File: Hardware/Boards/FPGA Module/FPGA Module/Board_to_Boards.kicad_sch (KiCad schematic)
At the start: 0 parts

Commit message: FPGA Board schematic work
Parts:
- added J1, J2: LSHM-130-XX.X-XXX-DV-A-S-K-XX, FPGA Module:SAMTEC_LSHM-130-XX.X-XXX-DV-A-S-K-XX, symbol FPGA Module:LSHM-130-XX.X-XXX-DV-A-S-K-XX

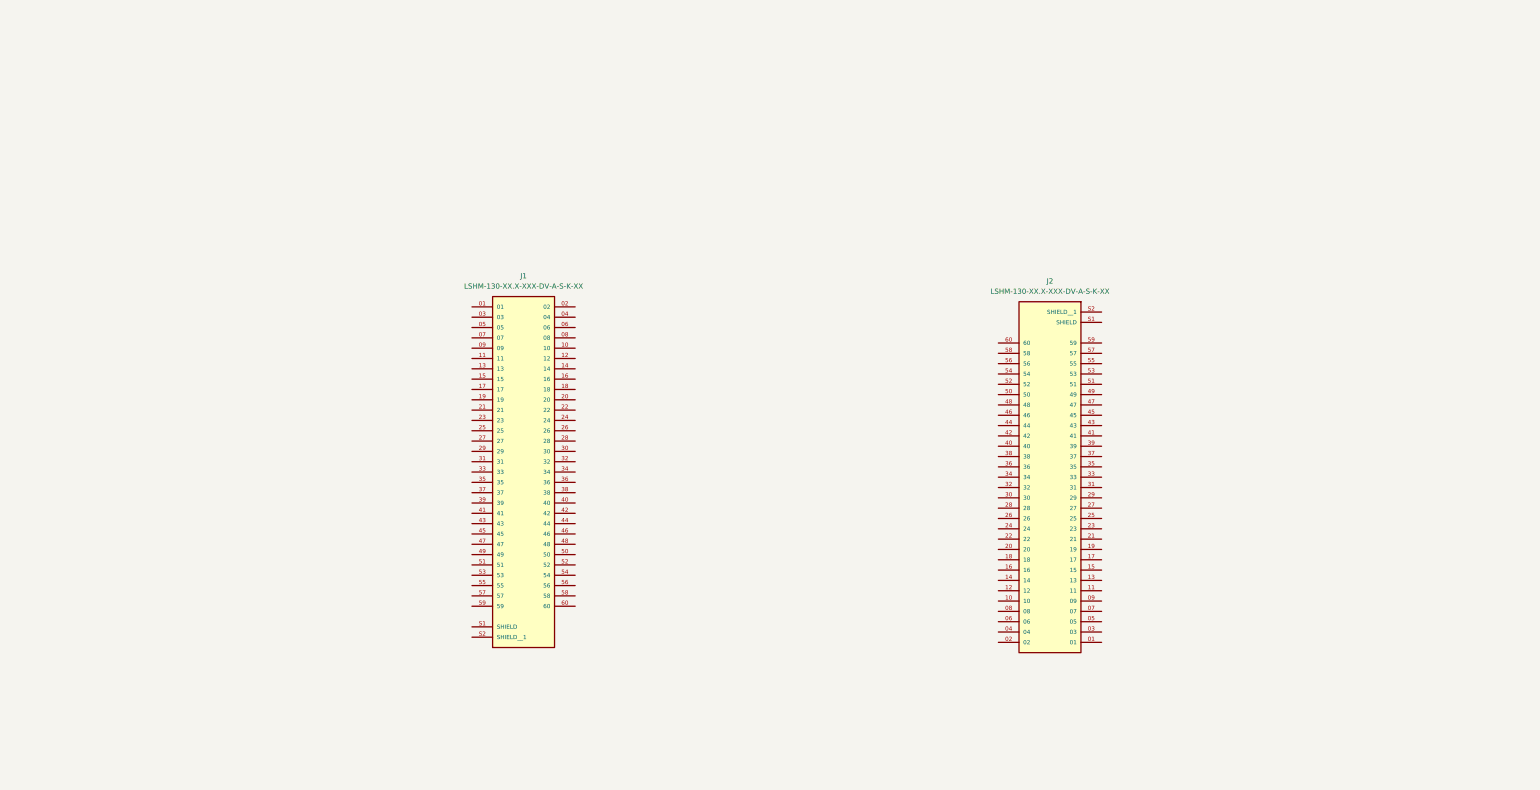
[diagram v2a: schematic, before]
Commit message: FPGA Module Schematic work
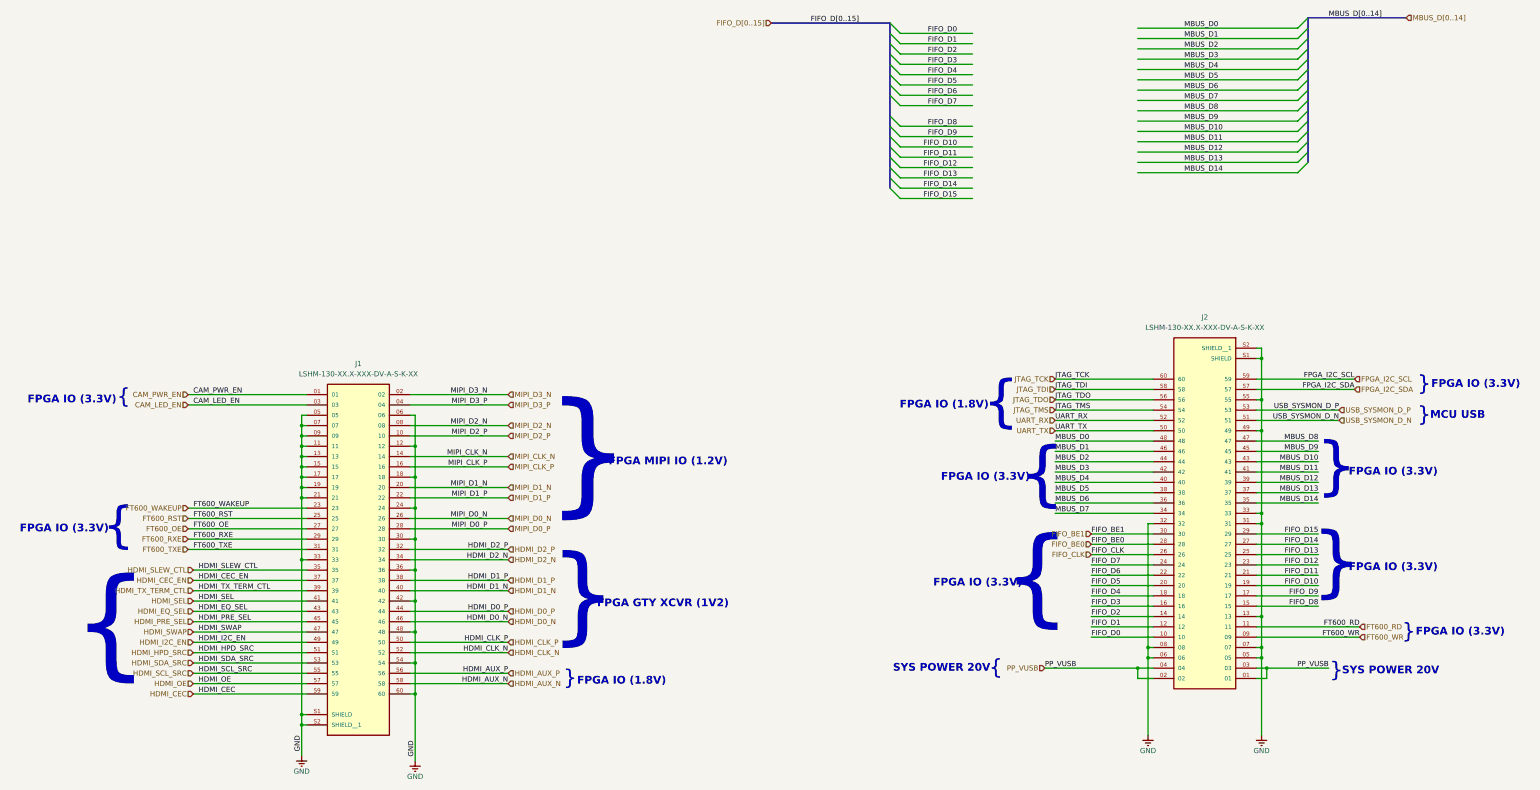
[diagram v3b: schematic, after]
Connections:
- net PP_VUSB: now reaches J2.01
- net PP_VUSB: now also J2.02, J2.03, J2.04
- net GND: now reaches J2.05
- net GND: now also J1.05, J1.06, J1.07, J1.09, J1.11, J1.12, J1.13, J1.15, J1.17, J1.18, J1.19, J1.21, J1.24, J1.30, J1.33, J1.36, J1.42, J1.48, J1.54, J1.60, J1.S1 (SHIELD), J1.S2 (SHIELD__1), J2.06, J2.07, J2.08, J2.13, J2.31, J2.32, J2.33, J2.49, J2.55, J2.S1 (SHIELD), J2.S2 (SHIELD__1)
- net FT600_WR: now reaches J2.09
- net FIFO_D0: now reaches J2.10
- net FT600_RD: now reaches J2.11
- net FIFO_D1: now reaches J2.12
- net FIFO_D2: now reaches J2.14
- net FIFO_D8: now reaches J2.15
- net FIFO_D3: now reaches J2.16
- net FIFO_D9: now reaches J2.17
- net FIFO_D4: now reaches J2.18
- net FIFO_D10: now reaches J2.19
- net FIFO_D5: now reaches J2.20
- net FIFO_D11: now reaches J2.21
- net FIFO_D6: now reaches J2.22
- net FIFO_D12: now reaches J2.23
- net FIFO_D7: now reaches J2.24
- net FIFO_D13: now reaches J2.25
- net FIFO_CLK: now reaches J2.26
- net FIFO_D14: now reaches J2.27
- net FIFO_BE0: now reaches J2.28
- net FIFO_D15: now reaches J2.29
- net FIFO_BE1: now reaches J2.30
- net MBUS_D7: now reaches J2.34
- net MBUS_D14: now reaches J2.35
- net MBUS_D6: now reaches J2.36
- net MBUS_D13: now reaches J2.37
- net MBUS_D5: now reaches J2.38
- net MBUS_D12: now reaches J2.39
- net MBUS_D4: now reaches J2.40
- net MBUS_D11: now reaches J2.41
- net MBUS_D3: now reaches J2.42
- net MBUS_D10: now reaches J2.43
- net MBUS_D2: now reaches J2.44
- net MBUS_D9: now reaches J2.45
- net MBUS_D1: now reaches J2.46
- net MBUS_D8: now reaches J2.47
- net MBUS_D0: now reaches J2.48
- net UART_TX: now reaches J2.50
- net USB_SYSMON_D_N: now reaches J2.51
- net UART_RX: now reaches J2.52
- net USB_SYSMON_D_P: now reaches J2.53
- net JTAG_TMS: now reaches J2.54
- net JTAG_TDO: now reaches J2.56
- net FPGA_I2C_SDA: now reaches J2.57
- net JTAG_TDI: now reaches J2.58
- net FPGA_I2C_SCL: now reaches J2.59
- net JTAG_TCK: now reaches J2.60
- net CAM_PWR_EN: now reaches J1.01
- net MIPI_D3_N: now reaches J1.02
- net CAM_LED_EN: now reaches J1.03
- net MIPI_D3_P: now reaches J1.04
- net MIPI_D2_N: now reaches J1.08
- net MIPI_D2_P: now reaches J1.10
- net MIPI_CLK_N: now reaches J1.14
- net MIPI_CLK_P: now reaches J1.16
- net MIPI_D1_N: now reaches J1.20
- net MIPI_D1_P: now reaches J1.22
- net FT600_WAKEUP: now reaches J1.23
- net FT600_RST: now reaches J1.25
- net MIPI_D0_N: now reaches J1.26
- net FT600_OE: now reaches J1.27
- net MIPI_D0_P: now reaches J1.28
- net FT600_RXE: now reaches J1.29
- net FT600_TXE: now reaches J1.31
- net HDMI_D2_P: now reaches J1.32
- net HDMI_D2_N: now reaches J1.34
- net HDMI_SLEW_CTL: now reaches J1.35
- net HDMI_CEC_EN: now reaches J1.37
- net HDMI_D1_P: now reaches J1.38
- net HDMI_TX_TERM_CTL: now reaches J1.39
- net HDMI_D1_N: now reaches J1.40
- net HDMI_SEL: now reaches J1.41
- net HDMI_EQ_SEL: now reaches J1.43
- net HDMI_D0_P: now reaches J1.44
- net HDMI_PRE_SEL: now reaches J1.45
- net HDMI_D0_N: now reaches J1.46
- net HDMI_SWAP: now reaches J1.47
- net HDMI_I2C_EN: now reaches J1.49
- net HDMI_CLK_P: now reaches J1.50
- net HDMI_HPD_SRC: now reaches J1.51
- net HDMI_CLK_N: now reaches J1.52
- net HDMI_SDA_SRC: now reaches J1.53
- net HDMI_SCL_SRC: now reaches J1.55
- net HDMI_AUX_P: now reaches J1.56
- net HDMI_OE: now reaches J1.57
- net HDMI_AUX_N: now reaches J1.58
- net HDMI_CEC: now reaches J1.59
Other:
- note added: "FPGA GTY XCVR (1V2)"
- note added: "FPGA IO (1.8V)"
- note added: "FPGA IO (3.3V)"
- note added: "FPGA MIPI IO (1.2V)"
- note added: "MCU USB"
- note added: "SYS POWER 20V"
- note added: "{"
- note added: "}"
- moved on the sheet: J1, J2

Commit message: Using new DP to HDMI IC
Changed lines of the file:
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@@
+		)
+	)
+	(text "FPGA IO (1.8V)"
+		(exclude_from_sim no)
+		(at 34.29 177.8 0)
+		(effects
+			(font
+				(size 1.905 1.905)
+				(bold yes)
+			)
 		)
 	)

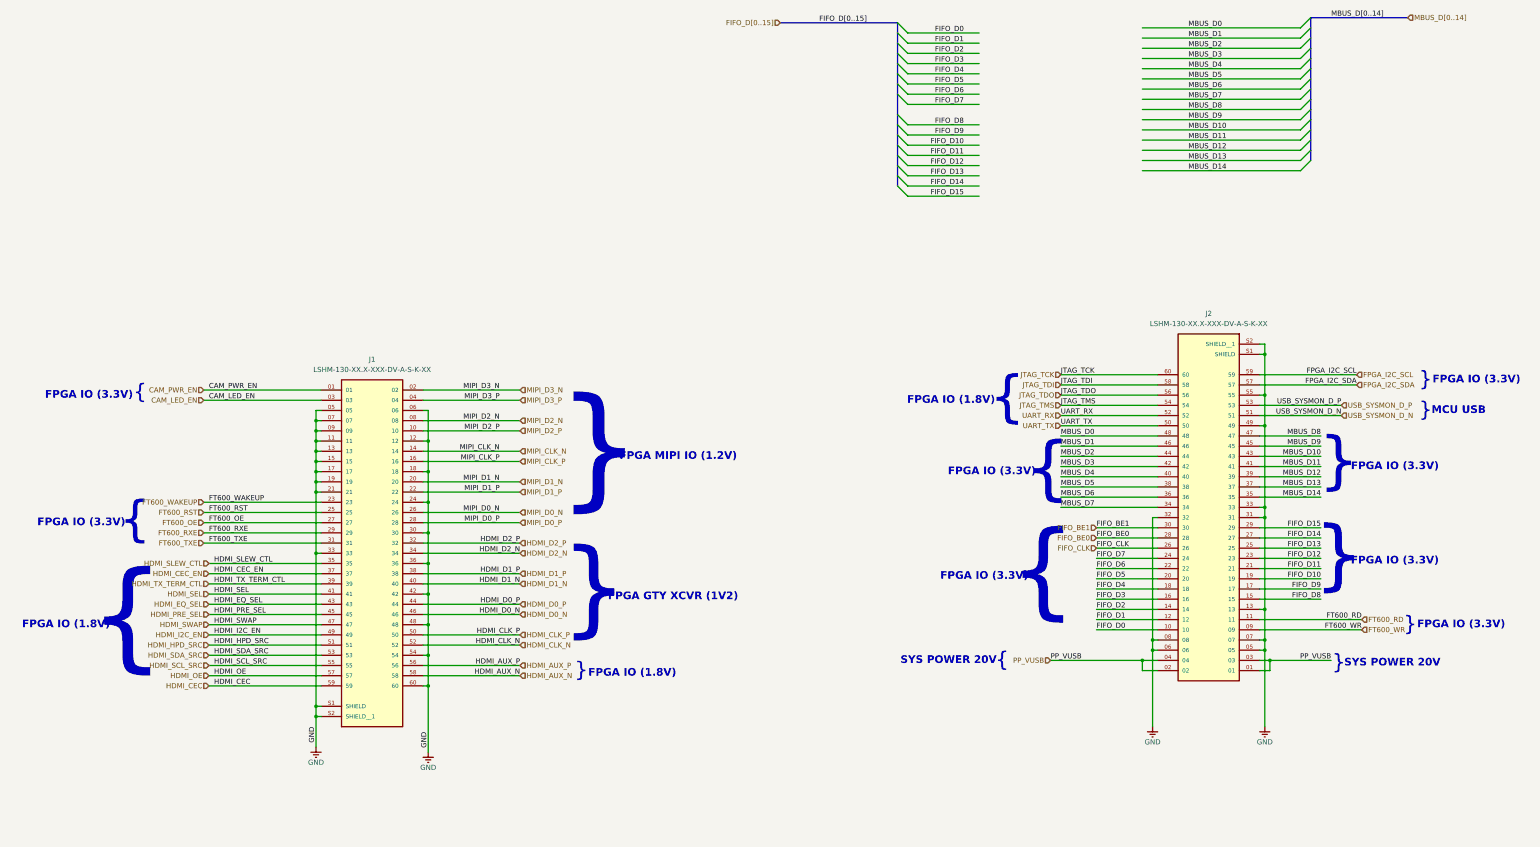
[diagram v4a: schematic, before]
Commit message: updated fpga module schematics
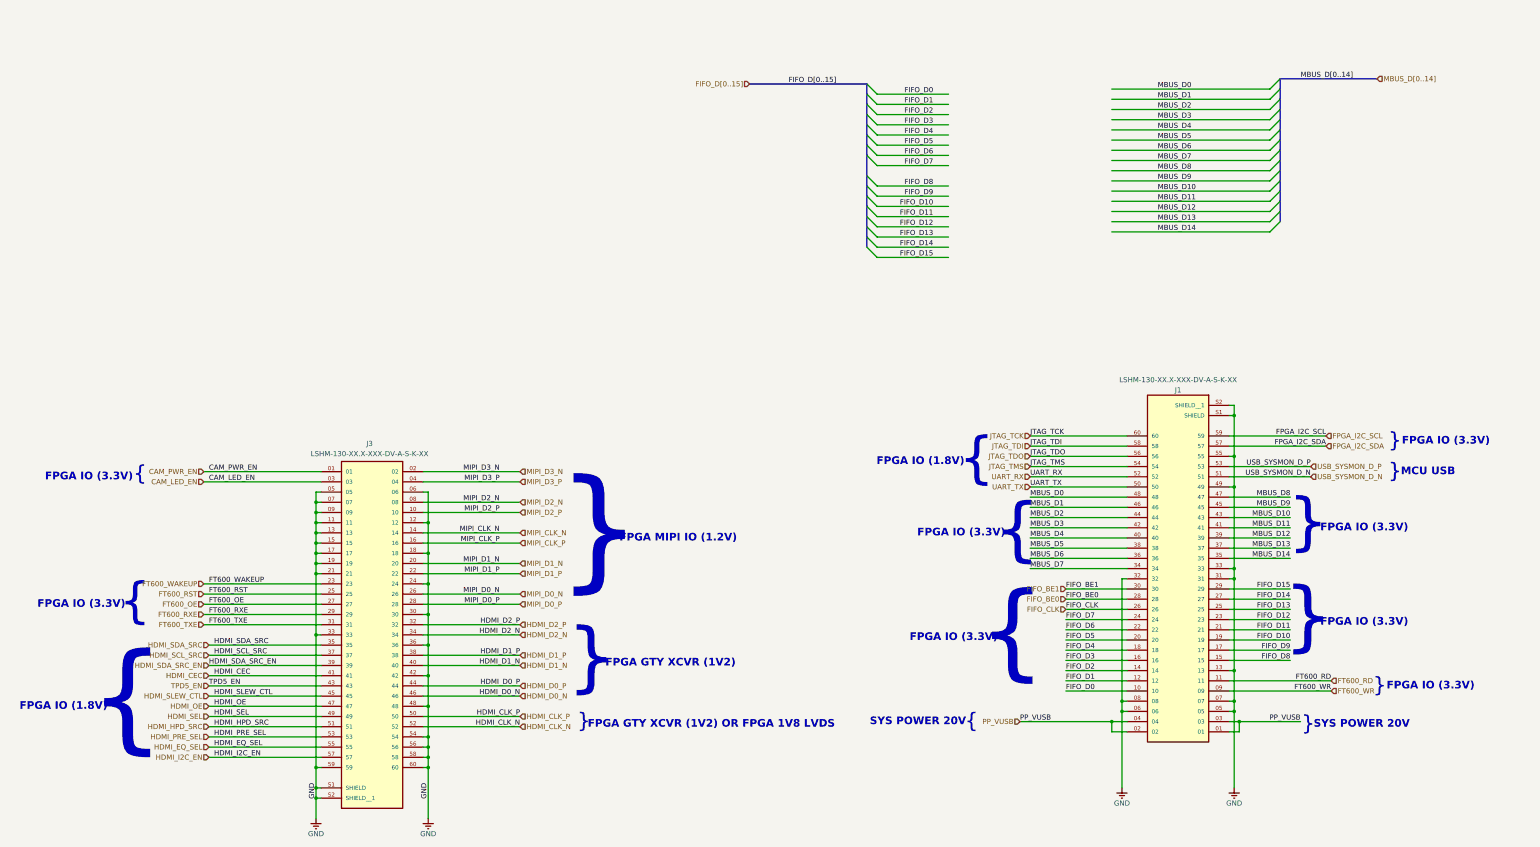
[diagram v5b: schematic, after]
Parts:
- removed J1, J2: LSHM-130-XX.X-XXX-DV-A-S-K-XX, FPGA Module:SAMTEC_LSHM-130-XX.X-XXX-DV-A-S-K-XX, symbol FPGA Module:LSHM-130-XX.X-XXX-DV-A-S-K-XX
- added J1, J3: LSHM-130-XX.X-XXX-DV-A-S-K-XX, IO_Module:SAMTEC_LSHM-130-XX.X-XXX-DV-A-S-K-XX, symbol IO_Module:LSHM-130-XX.X-XXX-DV-A-S-K-XX
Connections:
- net CAM_LED_EN: now also J3.03
- net CAM_PWR_EN: now also J3.01
- net FIFO_BE0: now also J1.28
- net FIFO_BE1: now also J1.30
- net FIFO_CLK: now also J1.26
- net FIFO_D0: now also J1.10
- net FIFO_D1: now also J1.12
- net FIFO_D10: now also J1.19
- net FIFO_D11: now also J1.21
- net FIFO_D12: now also J1.23
- net FIFO_D13: now also J1.25
- net FIFO_D14: now also J1.27
- net FIFO_D15: now also J1.29
- net FIFO_D2: now also J1.14
- net FIFO_D3: now also J1.16
- net FIFO_D4: now also J1.18
- net FIFO_D5: now also J1.20
- net FIFO_D6: now also J1.22
- net FIFO_D7: now also J1.24
- net FIFO_D8: now also J1.15
- net FIFO_D9: now also J1.17
- net FPGA_I2C_SCL: now also J1.59
- net FPGA_I2C_SDA: now also J1.57
- net FT600_OE: now also J3.27
- net FT600_RD: now also J1.11
- net FT600_RST: now also J3.25
- net FT600_RXE: now also J3.29
- net FT600_TXE: now also J3.31
- net FT600_WAKEUP: now also J3.23
- net FT600_WR: now also J1.09
- net GND: now also J1.05, J1.06, J1.07, J1.08, J1.13, J1.31, J1.32, J1.33, J1.49, J1.55, J1.S1 (SHIELD), J1.S2 (SHIELD__1), J3.05, J3.06, J3.07, J3.09, J3.11, J3.12, J3.13, J3.15, J3.17, J3.18, J3.19, J3.21, J3.24, J3.30, J3.33, J3.36, J3.42, J3.48, J3.54, J3.56, J3.58, J3.59, J3.60, J3.S1 (SHIELD), J3.S2 (SHIELD__1)
- net HDMI_CEC: now also J3.41
- net HDMI_CLK_N: now also J3.52
- net HDMI_CLK_P: now also J3.50
- net HDMI_D0_N: now also J3.46
- net HDMI_D0_P: now also J3.44
- net HDMI_D1_N: now also J3.40
- net HDMI_D1_P: now also J3.38
- net HDMI_D2_N: now also J3.34
- net HDMI_D2_P: now also J3.32
- net HDMI_EQ_SEL: now also J3.55
- net HDMI_HPD_SRC: now also J3.51
- net HDMI_I2C_EN: now also J3.57
- net HDMI_OE: now also J3.47
- net HDMI_PRE_SEL: now also J3.53
- net HDMI_SCL_SRC: now also J3.37
- net HDMI_SDA_SRC: now also J3.35
- net HDMI_SEL: now also J3.49
- net HDMI_SLEW_CTL: now also J3.45
- net JTAG_TCK: now also J1.60
- net JTAG_TDI: now also J1.58
- net JTAG_TDO: now also J1.56
- net JTAG_TMS: now also J1.54
- net MBUS_D0: now also J1.48
- net MBUS_D1: now also J1.46
- net MBUS_D10: now also J1.43
- net MBUS_D11: now also J1.41
- net MBUS_D12: now also J1.39
- net MBUS_D13: now also J1.37
- net MBUS_D14: now also J1.35
- net MBUS_D2: now also J1.44
- net MBUS_D3: now also J1.42
- net MBUS_D4: now also J1.40
- net MBUS_D5: now also J1.38
- net MBUS_D6: now also J1.36
- net MBUS_D7: now also J1.34
- net MBUS_D8: now also J1.47
- net MBUS_D9: now also J1.45
- net MIPI_CLK_N: now also J3.14
- net MIPI_CLK_P: now also J3.16
- net MIPI_D0_N: now also J3.26
- net MIPI_D0_P: now also J3.28
- net MIPI_D1_N: now also J3.20
- net MIPI_D1_P: now also J3.22
- net MIPI_D2_N: now also J3.08
- net MIPI_D2_P: now also J3.10
- net MIPI_D3_N: now also J3.02
- net MIPI_D3_P: now also J3.04
- net PP_VUSB: now also J1.01, J1.02, J1.03, J1.04
- net UART_RX: now also J1.52
- net UART_TX: now also J1.50
- net USB_SYSMON_D_N: now also J1.51
- net USB_SYSMON_D_P: now also J1.53
- new net HDMI_SDA_SRC_EN: J3.39
- new net TPD5_EN: J3.43
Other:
- note added: "FPGA GTY XCVR (1V2) OR FPGA 1V8 LVDS"

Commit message: Completed FPGA module PCB layout
Started PCB routing
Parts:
- J1: footprint IO_Module:SAMTEC_LSHM-130-XX.X-XXX-DV-A-S-K-XX -> FPGA Module:SAMTEC_LSHM-130-XX.X-XXX-DV-A-S-K-XX
- J2: renamed from J3; footprint IO_Module:SAMTEC_LSHM-130-XX.X-XXX-DV-A-S-K-XX -> FPGA Module:SAMTEC_LSHM-130-XX.X-XXX-DV-A-S-K-XX
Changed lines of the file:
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@@
 		(on_board yes)
 		(dnp no)
-		(property "Reference" "#PWR024"
+		(property "Reference" "#PWR0141"
 			(at 297.18 222.25 0)
 			(effects
@@
 			(project "FPGA Module"
 				(path "/199f10e2-d4b4-4a27-9e84-7b1ce2ae6bf0/0c296310-f788-47f0-8a3f-43c3444563e8/fe674990-db36-4599-87f6-ee1fee5b05ac"
-					(reference "#PWR024")
+					(reference "#PWR0141")
 					(unit 1)
 				)
@@
 		(on_board yes)
 		(dnp no)
-		(property "Reference" "#PWR0270"
+		(property "Reference" "#PWR0143"
 			(at 96.52 229.87 0)
 			(effects
@@
 			(project "FPGA Module"
 				(path "/199f10e2-d4b4-4a27-9e84-7b1ce2ae6bf0/0c296310-f788-47f0-8a3f-43c3444563e8/fe674990-db36-4599-87f6-ee1fee5b05ac"
-					(reference "#PWR0270")
+					(reference "#PWR0143")
 					(unit 1)
 				)
@@
 		(on_board yes)
 		(dnp no)
-		(property "Reference" "J3"
+		(property "Reference" "J2"
 			(at 109.855 132.715 0)
 			(effects
@@
 			)
 		)
-		(property "Footprint" "IO_Module:SAMTEC_LSHM-130-XX.X-XXX-DV-A-S-K-XX"
+		(property "Footprint" "FPGA Module:SAMTEC_LSHM-130-XX.X-XXX-DV-A-S-K-XX"
 			(at 110.49 180.34 0)
 			(effects
@@
 			(project "FPGA Module"
 				(path "/199f10e2-d4b4-4a27-9e84-7b1ce2ae6bf0/0c296310-f788-47f0-8a3f-43c3444563e8/fe674990-db36-4599-87f6-ee1fee5b05ac"
-					(reference "J3")
+					(reference "J2")
 					(unit 1)
 				)
@@
 		(on_board yes)
 		(dnp no)
-		(property "Reference" "#PWR025"
+		(property "Reference" "#PWR0142"
 			(at 325.12 222.25 0)
 			(effects
@@
 			(project "FPGA Module"
 				(path "/199f10e2-d4b4-4a27-9e84-7b1ce2ae6bf0/0c296310-f788-47f0-8a3f-43c3444563e8/fe674990-db36-4599-87f6-ee1fee5b05ac"
-					(reference "#PWR025")
+					(reference "#PWR0142")
 					(unit 1)
 				)
@@
 		(on_board yes)
 		(dnp no)
-		(property "Reference" "#PWR0271"
+		(property "Reference" "#PWR0144"
 			(at 124.46 229.87 0)
 			(effects
@@
 			(project "FPGA Module"
 				(path "/199f10e2-d4b4-4a27-9e84-7b1ce2ae6bf0/0c296310-f788-47f0-8a3f-43c3444563e8/fe674990-db36-4599-87f6-ee1fee5b05ac"
-					(reference "#PWR0271")
+					(reference "#PWR0144")
 					(unit 1)
 				)
@@
 			)
 		)
-		(property "Footprint" "IO_Module:SAMTEC_LSHM-130-XX.X-XXX-DV-A-S-K-XX"
+		(property "Footprint" "FPGA Module:SAMTEC_LSHM-130-XX.X-XXX-DV-A-S-K-XX"
 			(at 311.15 163.83 0)
 			(effects
